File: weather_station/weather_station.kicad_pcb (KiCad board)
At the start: 2 copper layers, 12 parts, among them J1 RJ11-6, J2 RJ11-6, J3 1935161, U1 BME280, U2 ESP32-DEVKITC-32D

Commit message: schematic and pcb updates
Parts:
- added C1: 10pF, Capacitor_SMD:C_0603_1608Metric_Pad1.05x0.95mm_HandSolder, F.Cu at (122.3, 64.3)
- added R3: 100k, Resistor_SMD:R_0603_1608Metric_Pad1.05x0.95mm_HandSolder, F.Cu at (122.3, 66.8)
- added R4: 100k, Resistor_SMD:R_0603_1608Metric_Pad1.05x0.95mm_HandSolder, F.Cu at (126.7, 64.3)
- added R5: 4.7k, Resistor_SMD:R_0603_1608Metric_Pad1.05x0.95mm_HandSolder, F.Cu at (126.7, 66.8)
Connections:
- J1 pad 1: Net-(J1-Pad1) -> GND
- J1 pad 2: Net-(J1-Pad2) -> GND
- J1 pad 3: Net-(J1-Pad3) -> /RAIN
- J1 pad 5: Net-(J1-Pad5) -> GND
- J1 pad 6: Net-(J1-Pad6) -> GND
- J2 pad 1: Net-(J2-Pad1) -> GND
- J2 pad 2: Net-(J2-Pad2) -> GND
- J2 pad 3: Net-(J2-Pad3) -> GND
- J2 pad 4: Net-(J2-Pad4) -> /WIND_SPD
- J2 pad 5: Net-(J2-Pad5) -> /WIND_DIR
- U2 pad 22: /SDA -> /SCL
- U2 pad 25: /SCL -> /SDA
- U2 pad 5: Net-(U2-Pad5) -> /RAIN
- U2 pad 6: Net-(J1-Pad3) -> /WIND_DIR
- U2 pad 7: Net-(U2-Pad7) -> /WIND_SPD

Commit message: more pcb update
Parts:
- added C3: 10pF, Capacitor_SMD:C_0603_1608Metric_Pad1.05x0.95mm_HandSolder, F.Cu at (118.1, 59.7)
- moved H2 42.6 mm to (180.3, 135.9)
- moved H3 42.6 mm to (180.3, 64.8)
- moved C1 42.6 mm to (163.0, 51.6)
- moved H1 42.6 mm to (94.0, 63.5)
- moved H4 42.6 mm to (94.0, 135.9)
- moved R3 42.6 mm to (163.0, 54.1)
- moved R4 42.6 mm to (167.3, 51.6)
- moved R5 42.6 mm to (167.3, 54.1)
- moved U2 42.6 mm to (139.3, 99.8)
- moved J1 42.6 mm to (92.7, 86.4)
- moved J2 42.6 mm to (92.7, 104.1)
- moved J3 42.6 mm to (90.2, 123.2)
- moved C2 42.6 mm to (194.0, 73.1)
- moved R1 42.6 mm to (206.1, 88.9)
- moved R2 42.6 mm to (179.1, 94.0)
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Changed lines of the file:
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@@
     (tracks 0)
     (zones 0)
-    (modules 16)
+    (modules 17)
     (nets 40)
   )
@@
     (add_net VDD)
   )
+  (module Capacitor_SMD:C_0603_1608Metric_Pad1.05x0.95mm_HandSolder (layer F.Cu)
+    (at 118.11 59.69)
+    (descr "Capacitor SMD 0603 (1608 Metric), square (rectangular) end terminal, IPC_7351 nominal with elongated pad for handsoldering. (Body size source: http://www.tortai-tech.com/upload/download/2011102023233369053.pdf), generated with kicad-footprint-generator")
+    (tags "capacitor handsolder")
+    (attr smd)
+    (fp_text reference C3 (at 0 -1.43) (layer F.SilkS)
+      (effects (font (size 1 1) (thickness 0.15)))
+    )
+    (fp_text value 10pF (at 0 1.43) (layer F.Fab)
+      (effects (font (size 1 1) (thickness 0.15)))
+    )
+    (fp_text user %R (at 0 0) (layer F.Fab)
+      (effects (font (size 0.4 0.4) (thickness 0.06)))
+    )
+    (fp_line (start -0.8 0.4) (end -0.8 -0.4) (layer F.Fab) (width 0.1))
+    (fp_line (start -0.8 -0.4) (end 0.8 -0.4) (layer F.Fab) (width 0.1))
+    (fp_line (start 0.8 -0.4) (end 0.8 0.4) (layer F.Fab) (width 0.1))
+    (fp_line (start 0.8 0.4) (end -0.8 0.4) (layer F.Fab) (width 0.1))
+    (fp_line (start -0.171267 -0.51) (end 0.171267 -0.51) (layer F.SilkS) (width 0.12))
+    (fp_line (start -0.171267 0.51) (end 0.171267 0.51) (layer F.SilkS) (width 0.12))
+    (fp_line (start -1.65 0.73) (end -1.65 -0.73) (layer F.CrtYd) (width 0.05))
+    (fp_line (start -1.65 -0.73) (end 1.65 -0.73) (layer F.CrtYd) (width 0.05))
+    (fp_line (start 1.65 -0.73) (end 1.65 0.73) (layer F.CrtYd) (width 0.05))
+    (fp_line (start 1.65 0.73) (end -1.65 0.73) (layer F.CrtYd) (width 0.05))
+    (pad 2 smd roundrect (at 0.875 0) (size 1.05 0.95) (layers F.Cu F.Paste F.Mask) (roundrect_rratio 0.25)
+      (net 2 GND))
+    (pad 1 smd roundrect (at -0.875 0) (size 1.05 0.95) (layers F.Cu F.Paste F.Mask) (roundrect_rratio 0.25)
+      (net 39 /WIND_SPD))
+    (model ${KISYS3DMOD}/Capacitor_SMD.3dshapes/C_0603_1608Metric.wrl
+      (at (xyz 0 0 0))
+      (scale (xyz 1 1 1))
+      (rotate (xyz 0 0 0))
+    )
+  )
   (module Resistor_SMD:R_0603_1608Metric_Pad1.05x0.95mm_HandSolder (layer F.Cu)
-    (at 126.675001 66.765001)
+    (at 167.315001 54.065001)
     (descr "Resistor SMD 0603 (1608 Metric), square (rectangular) end terminal, IPC_7351 nominal with elongated pad for handsoldering. (Body size source: http://www.tortai-tech.com/upload/download/2011102023233369053.pdf), generated with kicad-footprint-generator")
     (tags "resistor handsolder")
@@
   )
   (module Resistor_SMD:R_0603_1608Metric_Pad1.05x0.95mm_HandSolder (layer F.Cu)
-    (at 126.675001 64.255001)
+    (at 167.315001 51.555001)
     (descr "Resistor SMD 0603 (1608 Metric), square (rectangular) end terminal, IPC_7351 nominal with elongated pad for handsoldering. (Body size source: http://www.tortai-tech.com/upload/download/2011102023233369053.pdf), generated with kicad-footprint-generator")
     (tags "resistor handsolder")
@@
   )
   (module Resistor_SMD:R_0603_1608Metric_Pad1.05x0.95mm_HandSolder (layer F.Cu)
-    (at 122.325001 66.765001)
+    (at 162.965001 54.065001)
     (descr "Resistor SMD 0603 (1608 Metric), square (rectangular) end terminal, IPC_7351 nominal with elongated pad for handsoldering. (Body size source: http://www.tortai-tech.com/upload/download/2011102023233369053.pdf), generated with kicad-footprint-generator")
     (tags "resistor handsolder")
@@
   )
   (module Capacitor_SMD:C_0603_1608Metric_Pad1.05x0.95mm_HandSolder (layer F.Cu)
-    (at 122.325001 64.255001)
+    (at 162.965001 51.555001)
     (descr "Capacitor SMD 0603 (1608 Metric), square (rectangular) end terminal, IPC_7351 nominal with elongated pad for handsoldering. (Body size source: http://www.tortai-tech.com/upload/download/2011102023233369053.pdf), generated with kicad-footprint-generator")
     (tags "capacitor handsolder")
@@
   )
   (module Capacitor_SMD:C_0603_1608Metric_Pad1.05x0.95mm_HandSolder (layer F.Cu)
-    (at 153.365001 85.845001)
+    (at 194.005001 73.145001)
     (descr "Capacitor SMD 0603 (1608 Metric), square (rectangular) end terminal, IPC_7351 nominal with elongated pad for handsoldering. (Body size source: http://www.tortai-tech.com/upload/download/2011102023233369053.pdf), generated with kicad-footprint-generator")
     (tags "capacitor handsolder")
@@
   )
   (module MountingHole:MountingHole_3.2mm_M3_Pad (layer F.Cu)
-    (at 53.34 76.2)
+    (at 93.98 63.5)
     (descr "Mounting Hole 3.2mm, M3")
     (tags "mounting hole 3.2mm m3")
@@
   )
   (module MountingHole:MountingHole_3.2mm_M3_Pad (layer F.Cu)
-    (at 139.7 148.59)
+    (at 180.34 135.89)
     (descr "Mounting Hole 3.2mm, M3")
     (tags "mounting hole 3.2mm m3")
@@
   )
   (module MountingHole:MountingHole_3.2mm_M3_Pad (layer F.Cu)
-    (at 139.7 77.47)
+    (at 180.34 64.77)
     (descr "Mounting Hole 3.2mm, M3")
     (tags "mounting hole 3.2mm m3")
@@
   )
   (module MountingHole:MountingHole_3.2mm_M3_Pad (layer F.Cu)
-    (at 53.34 148.59)
+    (at 93.98 135.89)
     (descr "Mounting Hole 3.2mm, M3")
     (tags "mounting hole 3.2mm m3")
@@
   )
   (module Connectors:RJ11-6 (layer F.Cu)
-    (at 52.07 99.06 270)
+    (at 92.71 86.36 270)
     (descr "RJ11 6-PIN SOCKET WITH PCB MOUNTING POST")
     (tags "RJ11 6-PIN SOCKET WITH PCB MOUNTING POST")
@@
   )
   (module Connectors:RJ11-6 (layer F.Cu)
-    (at 52.07 116.84 270)
+    (at 92.71 104.14 270)
     (descr "RJ11 6-PIN SOCKET WITH PCB MOUNTING POST")
     (tags "RJ11 6-PIN SOCKET WITH PCB MOUNTING POST")
@@
   )
   (module TerminalBlock_Phoenix:TerminalBlock_Phoenix_MKDS-1,5-2_1x02_P5.00mm_Horizontal (layer F.Cu)
-    (at 49.53 135.89 90)
+    (at 90.17 123.19 90)
     (descr "Terminal Block Phoenix MKDS-1,5-2, 2 pins, pitch 5mm, size 10x9.8mm^2, drill diamater 1.3mm, pad diameter 2.6mm, see http://www.farnell.com/datasheets/100425.pdf, script-generated using https://github.com/pointhi/kicad-footprint-generator/scripts/TerminalBlock_Phoenix")
     (tags "THT Terminal Block Phoenix MKDS-1,5-2 pitch 5mm size 10x9.8mm^2 drill 1.3mm pad 2.6mm")
@@
   )
   (module Resistor_SMD:R_0603_1608Metric_Pad1.05x0.95mm_HandSolder (layer F.Cu)
-    (at 165.495 101.6)
+    (at 206.135 88.9)
     (descr "Resistor SMD 0603 (1608 Metric), square (rectangular) end terminal, IPC_7351 nominal with elongated pad for handsoldering. (Body size source: http://www.tortai-tech.com/upload/download/2011102023233369053.pdf), generated with kicad-footprint-generator")
     (tags "resistor handsolder")
@@
   )
   (module Resistor_SMD:R_0603_1608Metric_Pad1.05x0.95mm_HandSolder (layer F.Cu)
-    (at 138.43 106.68)
+    (at 179.07 93.98)
     (descr "Resistor SMD 0603 (1608 Metric), square (rectangular) end terminal, IPC_7351 nominal with elongated pad for handsoldering. (Body size source: http://www.tortai-tech.com/upload/download/2011102023233369053.pdf), generated with kicad-footprint-generator")
     (tags "resistor handsolder")
@@
   )
   (module digikey-footprints:Pressure_Sensor_LGA-8_2.5x2.5mm_BME280 (layer F.Cu)
-    (at 148.59 100.33)
+    (at 189.23 87.63)
     (attr smd)
     (fp_text reference U1 (at 0 -2.3) (layer F.SilkS)
@@
   )
   (module weather_station:MODULE_ESP32-DEVKITC-32D (layer F.Cu)
-    (at 98.700001 112.515001)
+    (at 139.340001 99.815001)
     (fp_text reference U2 (at -10.829175 -28.446045) (layer F.SilkS)
       (effects (font (size 1.000386 1.000386) (thickness 0.015)))

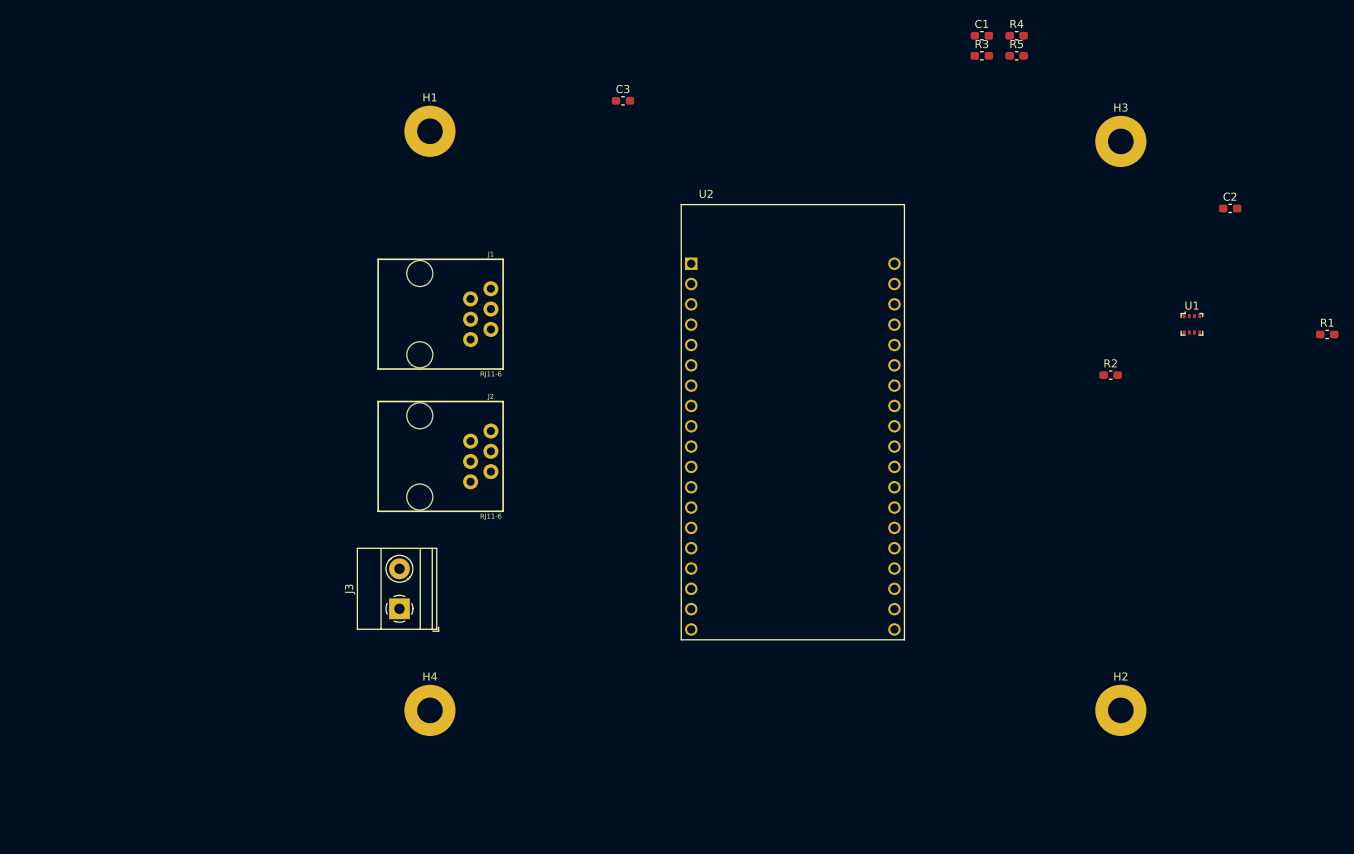
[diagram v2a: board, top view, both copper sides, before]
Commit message: pcb updates, dont use this the schematic is scuffed
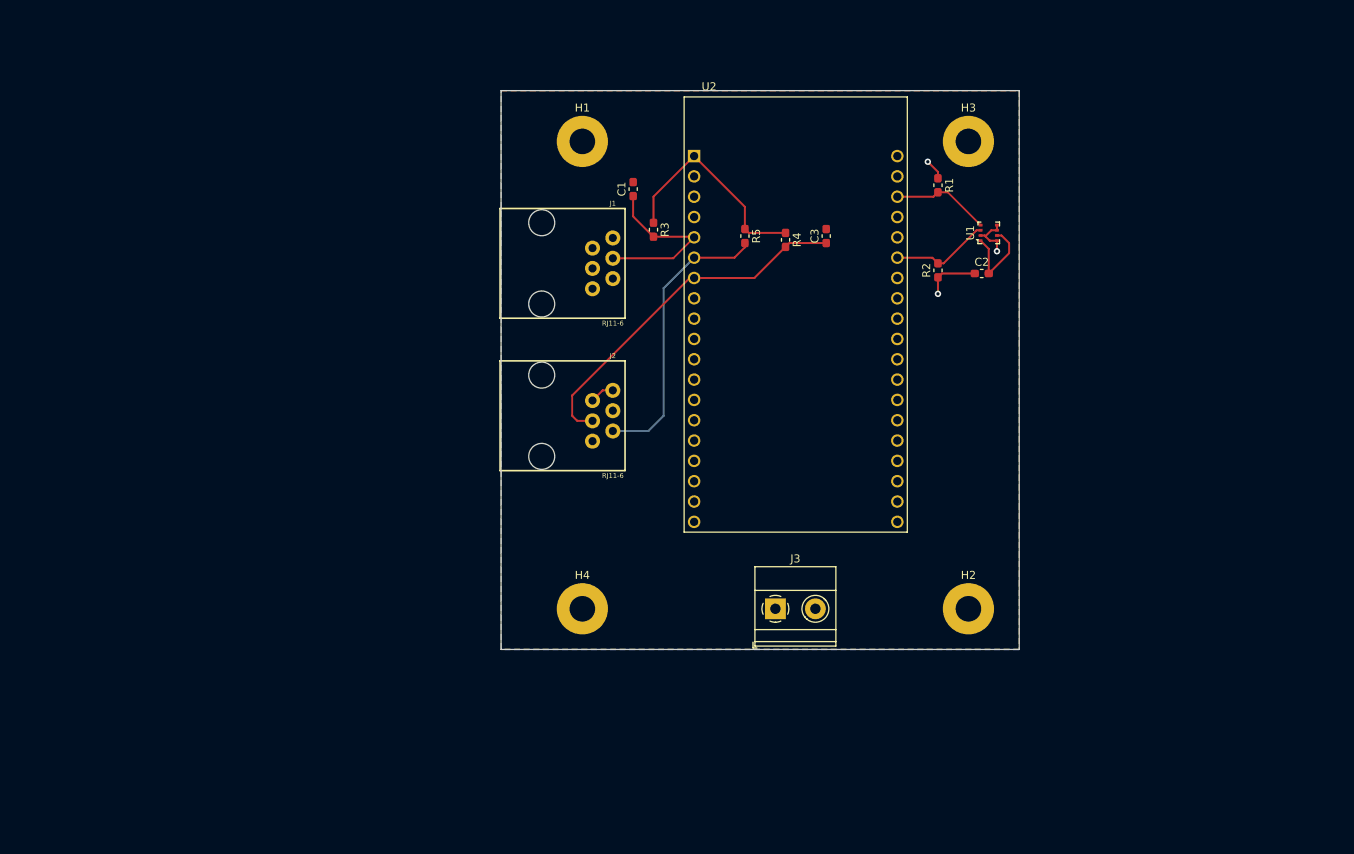
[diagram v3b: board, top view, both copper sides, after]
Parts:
- moved R1 52.1 mm to (157.5, 70.2), turned to 270 degrees
- moved C1 47.6 mm to (119.4, 70.7), turned to 90 degrees
- moved J3 47.0 mm to (137.2, 123.2), turned to 0 degrees
- moved R3 46.4 mm to (121.9, 75.8), turned to 270 degrees
- moved R5 40.8 mm to (133.3, 76.6), turned to 270 degrees
- moved R4 38.5 mm to (138.4, 77.1), turned to 270 degrees
- moved C2 32.1 mm to (163.0, 81.3)
- moved C3 30.5 mm to (143.5, 76.6), turned to 90 degrees
- moved U1 27.9 mm to (163.8, 76.2), turned to 90 degrees
- moved R2 25.3 mm to (157.5, 80.9), turned to 90 degrees
- moved H2 22.9 mm to (161.3, 123.2)
- moved H4 22.9 mm to (113.0, 123.2)
- moved H1 19.1 mm to (113.0, 64.8)
- moved H3 19.1 mm to (161.3, 64.8)
- moved J1 16.5 mm to (108.0, 80.0)
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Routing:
- net /WIND_SPD: track 0.00 -> 45.0 mm
- net VDD: track 0.00 -> 43.0 mm, vias 0 -> 3
- net /WIND_DIR: track 0.00 -> 35.9 mm
- net /RAIN: track 0.00 -> 22.5 mm
- net GND: track 0.00 -> 14.4 mm
- net /SDA: track 0.00 -> 12.4 mm
- net /SCL: track 0.00 -> 12.3 mm
- added copper zone on F.Cu, net GND
- added copper zone on B.Cu, net VDD
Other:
- board outline added: 64.8 x 69.9 mm

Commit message: pcb updates and some tiny code changes
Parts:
- added ?: , Aesthetics:OSHW-LOGO-L_COPPER, F.Cu at (111.8, 114.3)
- added C4: 100nF, Capacitor_SMD:C_0603_1608Metric_Pad1.08x0.95mm_HandSolder, F.Cu at (162.6, 100.3)
- added R6: 1k, Resistor_SMD:R_0603_1608Metric_Pad0.98x0.95mm_HandSolder, F.Cu at (157.5, 100.3)
- added U3: S35770, Package_SO:SSOP-8_5.25x5.24mm_P1.27mm, F.Cu at (160.0, 91.4)
- J1: value RJ11-6 -> 1935161; footprint Connectors:RJ11-6 -> TerminalBlock_Phoenix:TerminalBlock_Phoenix_MKDS-1,5-2_1x02_P5.00mm_Horizontal
- J2: value RJ11-6 -> Screw_Terminal_01x03; footprint Connectors:RJ11-6 -> TerminalBlock_Phoenix:TerminalBlock_Phoenix_MKDS-1,5-3_1x03_P5.00mm_Horizontal
- moved R4 32.8 mm to (121.9, 105.4), turned to 90 degrees
- moved C3 27.7 mm to (121.9, 94.0)
- moved R5 13.1 mm to (121.9, 82.9)
- moved J2 6.35 mm to (111.8, 94.0)
- moved J1 5.39 mm to (111.8, 76.2)
- moved C1 2.54 mm to (121.9, 70.7)
- moved R3 0.48 mm to (121.9, 75.3)
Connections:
- J1 pad 1: GND -> /RAIN
- J2 pad 2: GND -> /WIND_SPD
- J2 pad 3: GND -> /WIND_DIR
- U2 pad 1: VDD -> Net-(U2-Pad1)
- U2 pad 14: Net-(U2-Pad14) -> GND
- U2 pad 19: Net-(U2-Pad19) -> VDD
- U2 pad 26: Net-(U2-Pad26) -> GND
- U2 pad 7: /WIND_SPD -> Net-(U2-Pad7)
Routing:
- net VDD: track 43.0 -> 159.9 mm, vias 3 -> 2
- net /WIND_SPD: track 45.0 -> 99.1 mm, vias 0 -> 1
- net GND: track 14.4 -> 68.4 mm
- net /SDA: track 12.4 -> 28.6 mm, vias 0 -> 2
- net /SCL: track 12.3 -> 28.0 mm, vias 0 -> 2
- net /WIND_DIR: track 35.9 -> 43.7 mm, vias 0 -> 1
- net Net-(R6-Pad2): track 0.00 -> 6.21 mm
- net Net-(U2-Pad7): track 0.00 -> 0.56 mm
- added copper zone on B.Cu, net GND
- removed copper zone on F.Cu, net GND
- removed copper zone on B.Cu, net VDD
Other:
- board size 64.8 x 69.9 mm -> 63.5 x 69.9 mm
- board text added: "Rain Meter"
- board text added: "Wind Spd & Dir"
